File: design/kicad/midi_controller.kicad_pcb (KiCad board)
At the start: 2 copper layers, 166 x 166 mm, 19 parts, among them SW1 MIDI_Switch_Pushbutton_PV0H24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, SW2 MIDI_Switch_Pushbutton_PV0H24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, SW3 MIDI_Switch_Pushbutton_PV0H24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, SW4 MIDI_Switch_Pushbutton_PV0H24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, SW5 MIDI_Switch_Pushbutton_PV0H24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, SW6 MIDI_Switch_Pushbutton_PV0H24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, U1 CD74HC4067M

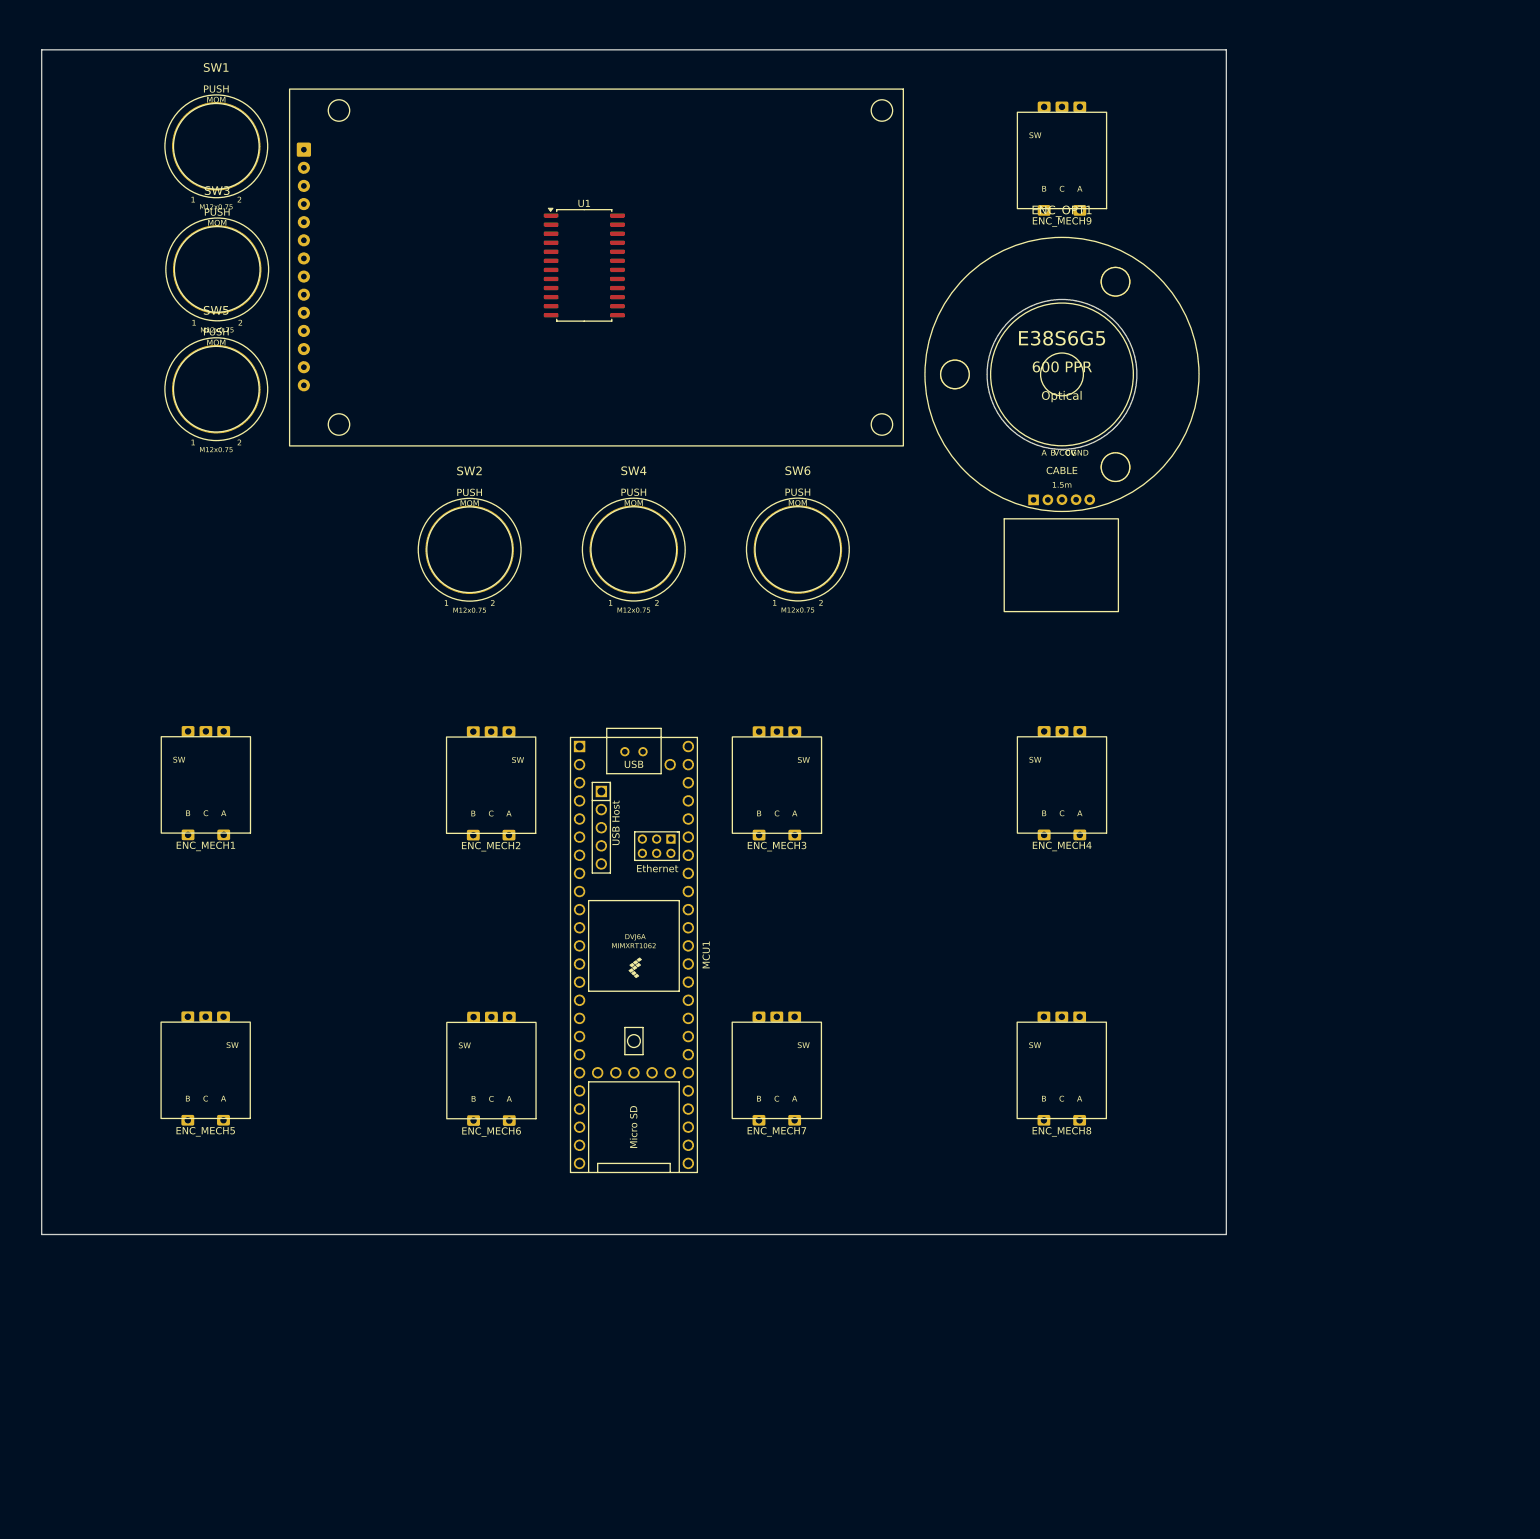
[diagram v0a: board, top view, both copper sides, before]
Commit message: Update kicad binary files - update 3d models
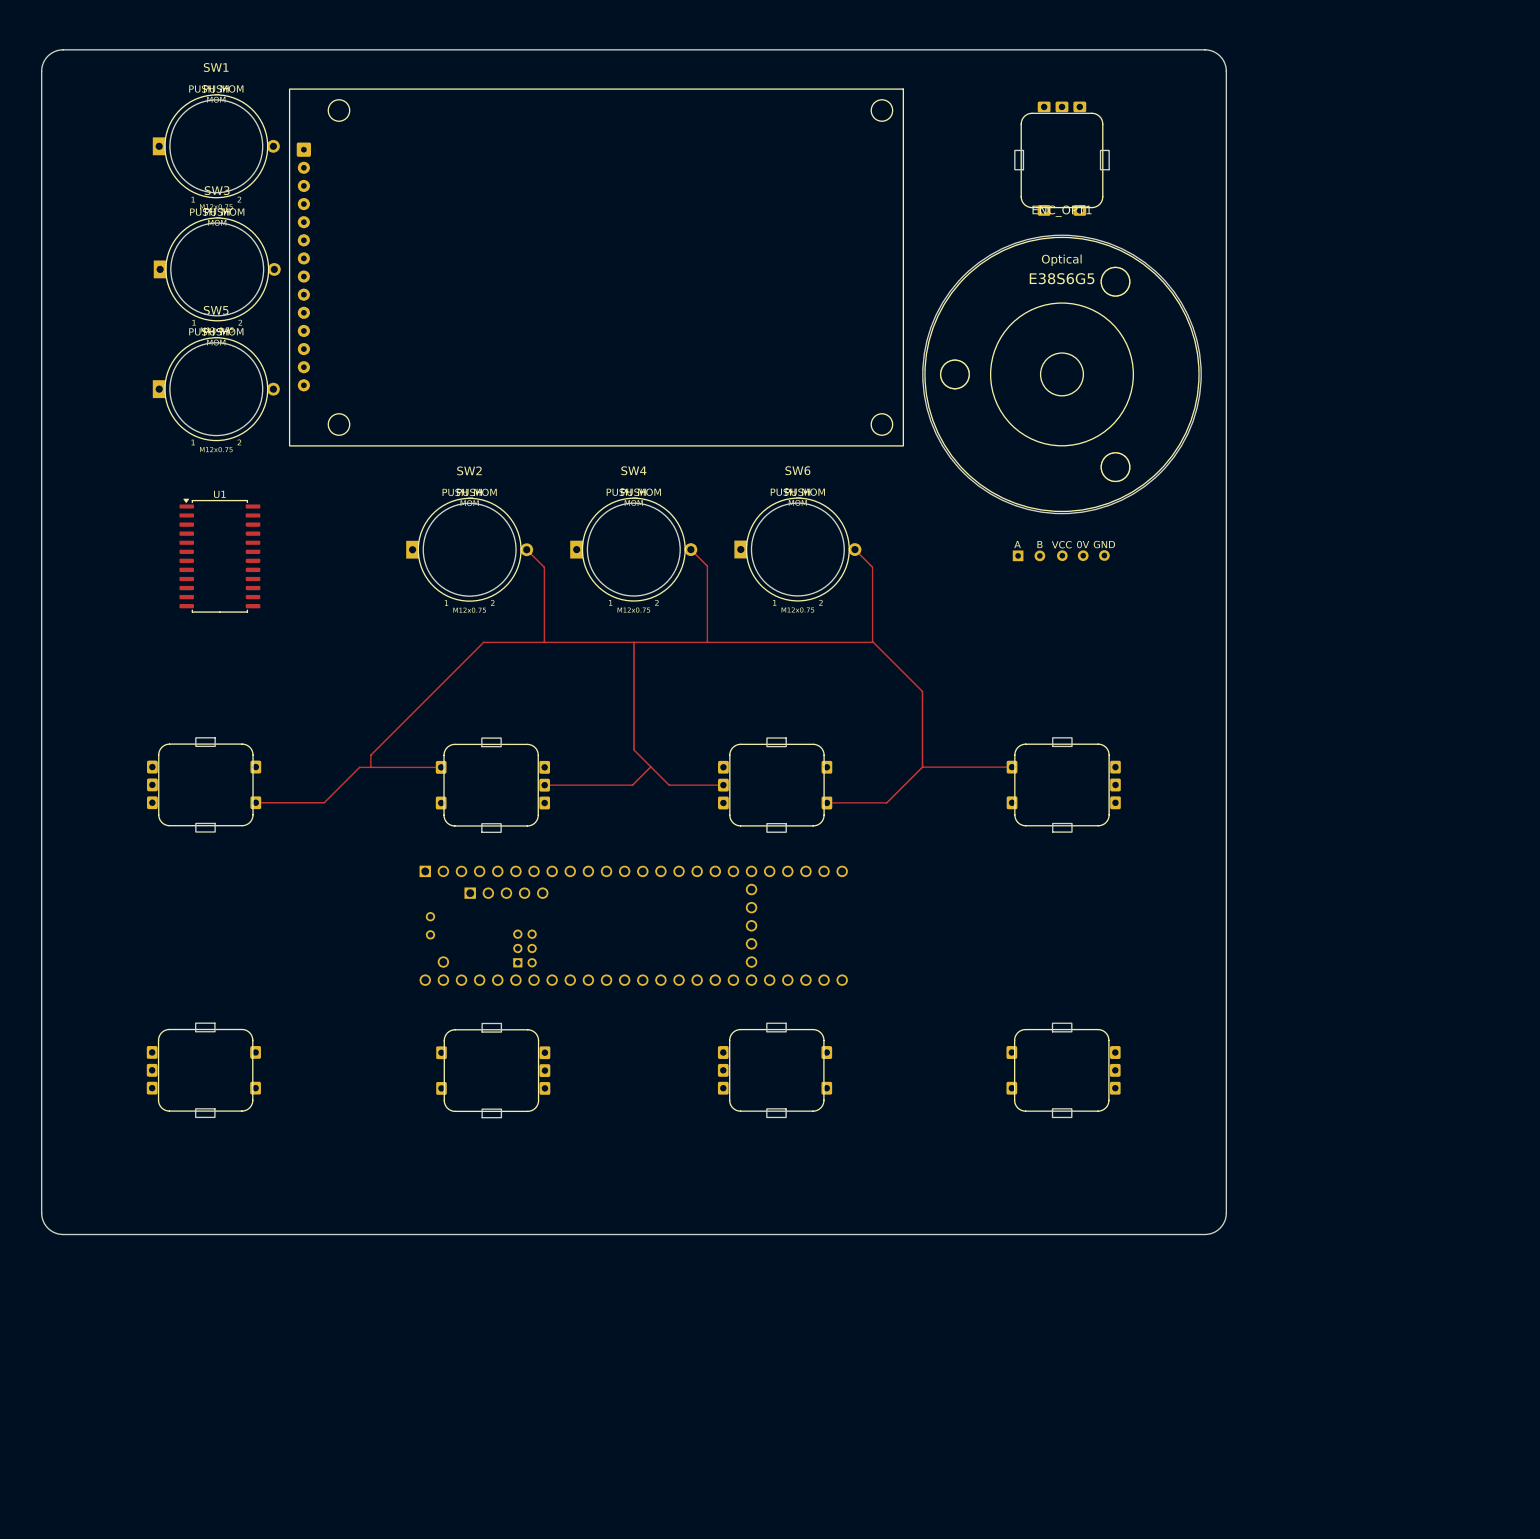
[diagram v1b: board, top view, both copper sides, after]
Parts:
- MCU1: moved to B.Cu
- moved U1 65.3 mm to (60.0, 107.3)
- moved MCU1 4.09 mm to (118.0, 159.1), turned to 0 degrees
- turned ENC_MECH1 to -90 degrees
- turned ENC_MECH2 to 90 degrees
- turned ENC_MECH3 to -90 degrees
- turned ENC_MECH4 to 90 degrees
- turned ENC_MECH5 to -90 degrees
- turned ENC_MECH6 to 90 degrees
- turned ENC_MECH7 to -90 degrees
- turned ENC_MECH8 to 90 degrees
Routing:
- net /Buttons_Momentary/GND: track 0.00 -> 242.6 mm
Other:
- outline, holes or cut-outs redrawn

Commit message: Update kicad binary files
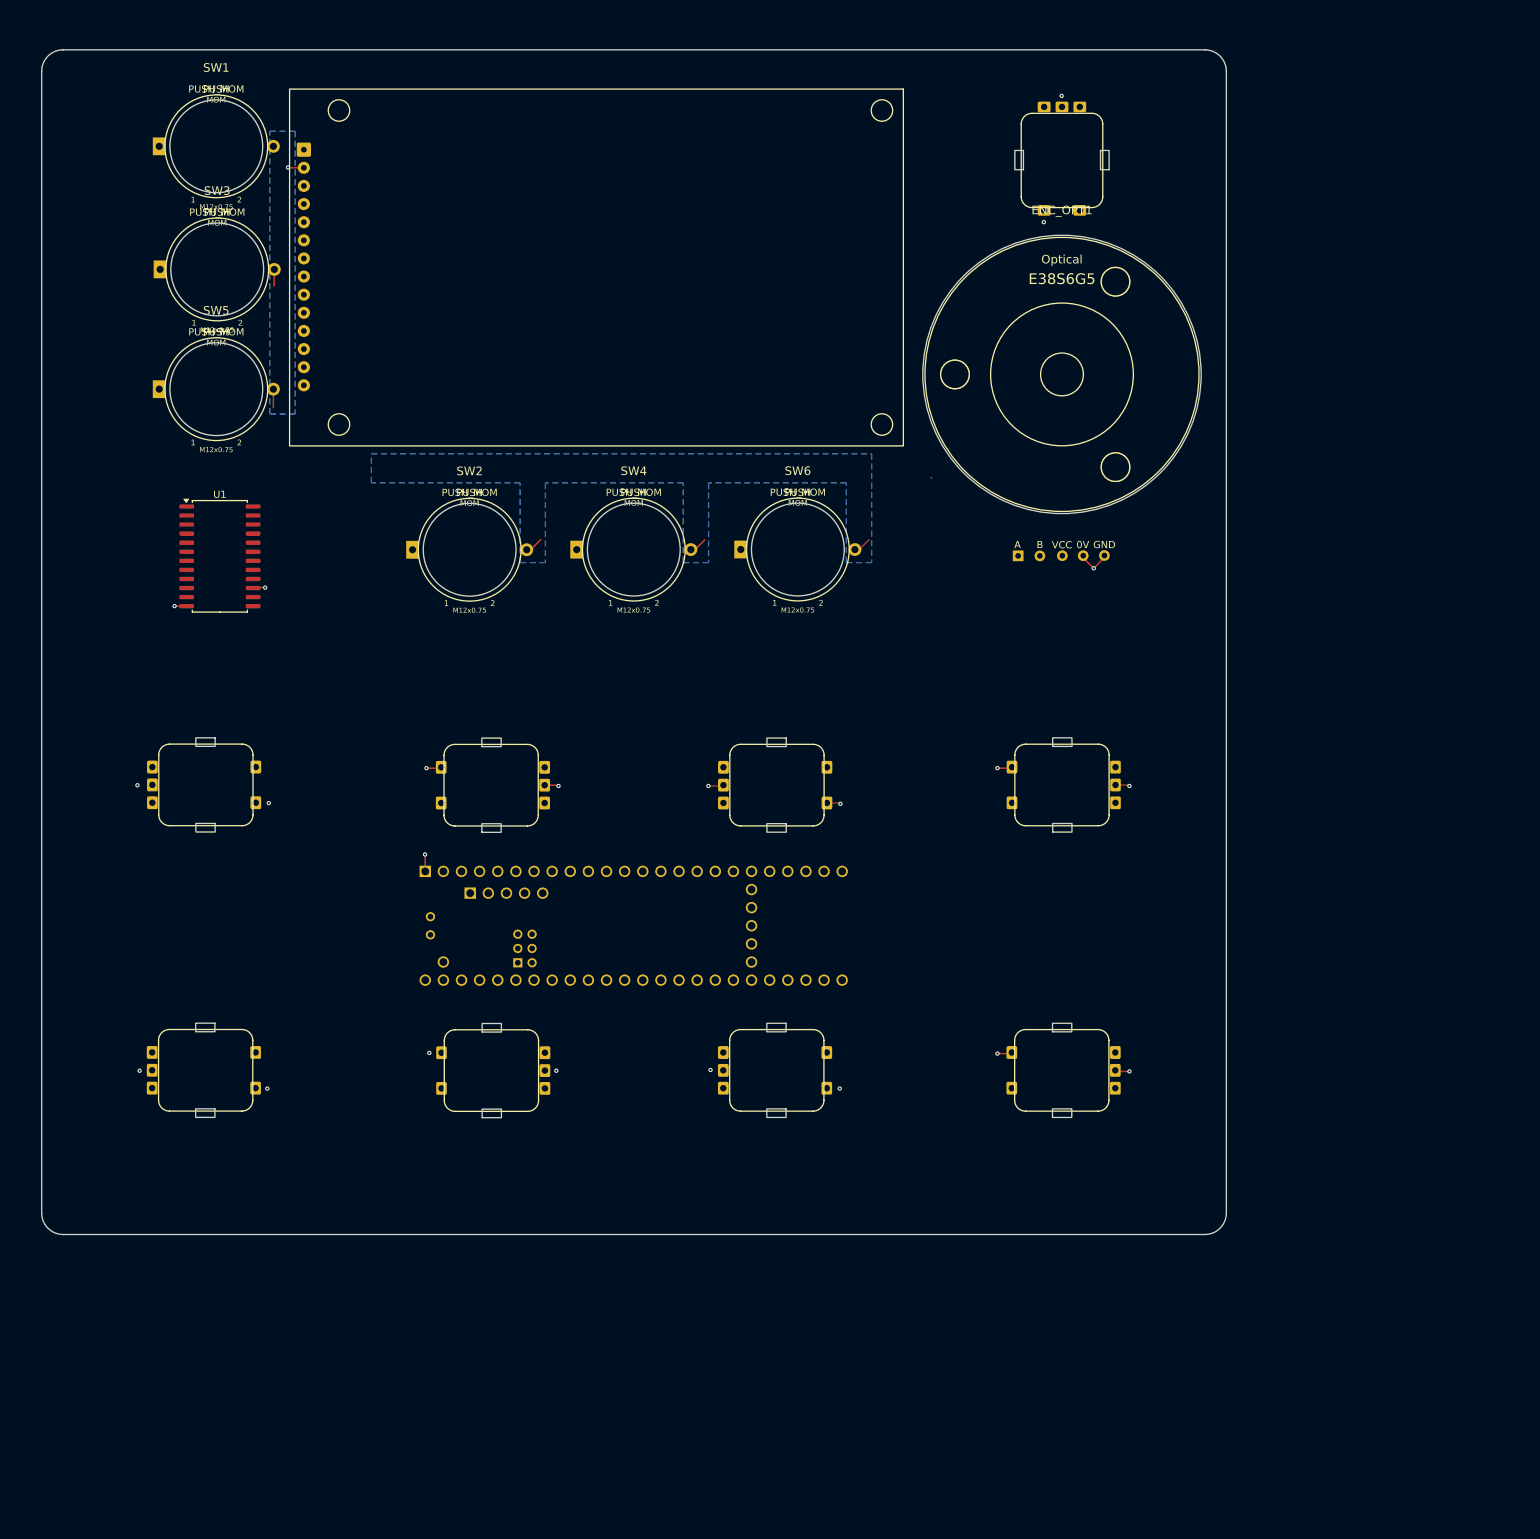
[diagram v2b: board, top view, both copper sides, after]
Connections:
- net /MIDI_Encoder_Matrix_2x4_with_push_buttons/1x1.QUAD_A renamed /MIDI_Encoder_Matrix_2x4_with_push_buttons/1x1.QUAD_B
- net /MIDI_Encoder_Matrix_2x4_with_push_buttons/1x2.QUAD_A renamed /MIDI_Encoder_Matrix_2x4_with_push_buttons/1x2.QUAD_B
- net /MIDI_Encoder_Matrix_2x4_with_push_buttons/1x3.QUAD_A renamed /MIDI_Encoder_Matrix_2x4_with_push_buttons/1x3.QUAD_B
- net /MIDI_Encoder_Matrix_2x4_with_push_buttons/1x4.QUAD_A renamed /MIDI_Encoder_Matrix_2x4_with_push_buttons/1x4.QUAD_B
- net /MIDI_Encoder_Matrix_2x4_with_push_buttons/2x1.QUAD_A renamed /MIDI_Encoder_Matrix_2x4_with_push_buttons/2x1.QUAD_B
- net /MIDI_Encoder_Matrix_2x4_with_push_buttons/2x2.QUAD_A renamed /MIDI_Encoder_Matrix_2x4_with_push_buttons/2x2.QUAD_B
- net /MIDI_Encoder_Matrix_2x4_with_push_buttons/2x3.QUAD_A renamed /MIDI_Encoder_Matrix_2x4_with_push_buttons/2x3.QUAD_B
- net /MIDI_Encoder_Matrix_2x4_with_push_buttons/2x4.QUAD_A renamed /MIDI_Encoder_Matrix_2x4_with_push_buttons/2x4.QUAD_B
- D1 pad 2: Net-(D1-GND) -> /Buttons_Momentary/GND
- ENC_OPT1 pad 0V: Net-(ENC_OPT1-Pad0V) -> /Buttons_Momentary/GND
- ENC_OPT1 pad GND: Net-(ENC_OPT1-Pad0V) -> /Buttons_Momentary/GND
- MCU1 pad 1: Net-(D1-GND) -> /Buttons_Momentary/GND
- MCU1 pad 34: Net-(ENC_OPT1-Pad0V) -> unconnected-(MCU1-GND-Pad34)
- MCU1 pad 47: /Buttons_Momentary/GND -> unconnected-(MCU1-GND-Pad47)
- U1 pad 24: unconnected-(U1-VCC-Pad24) -> Net-(D1-VCC)
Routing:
- net /Buttons_Momentary/GND: track 242.6 -> 42.0 mm, vias 0 -> 23
- added copper zone on B.Cu, net /Buttons_Momentary/GND
